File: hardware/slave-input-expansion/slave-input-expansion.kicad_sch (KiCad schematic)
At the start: 52 parts, among them J2 Conn_02x06_Odd_Even, J5 Conn_01x06, J6 ICSP, SW1 SW_Push, SW2 SW_Push, U3 PCF8574, U4 DS1233A-10

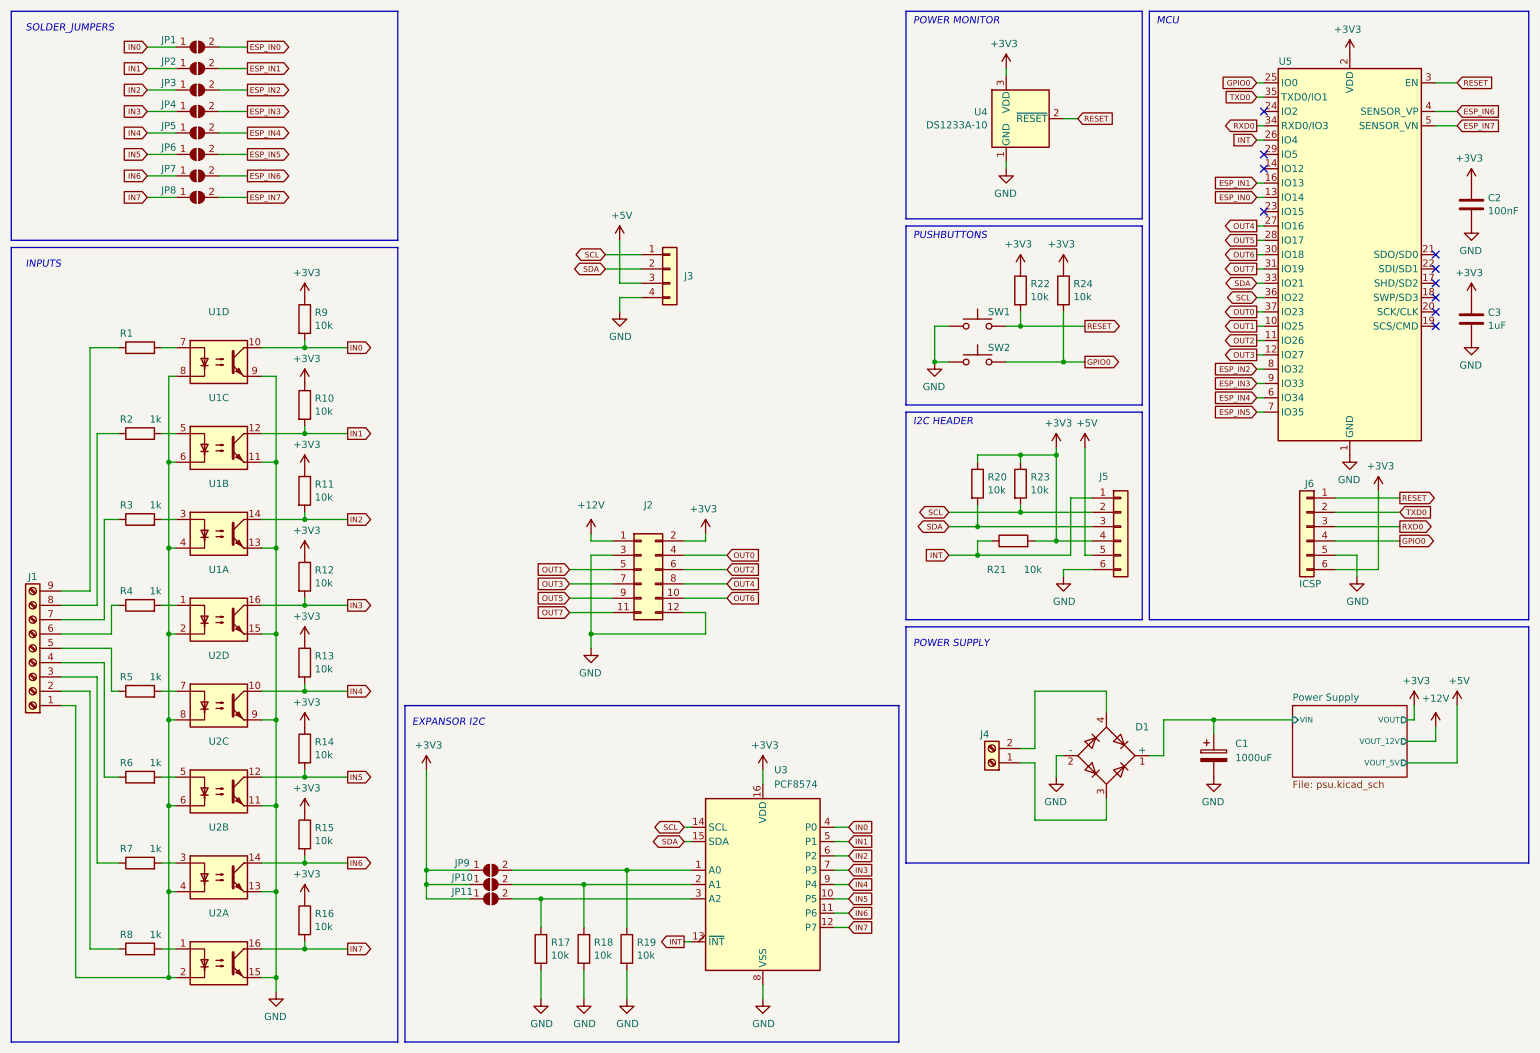
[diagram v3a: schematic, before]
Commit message: switch to 12v psu
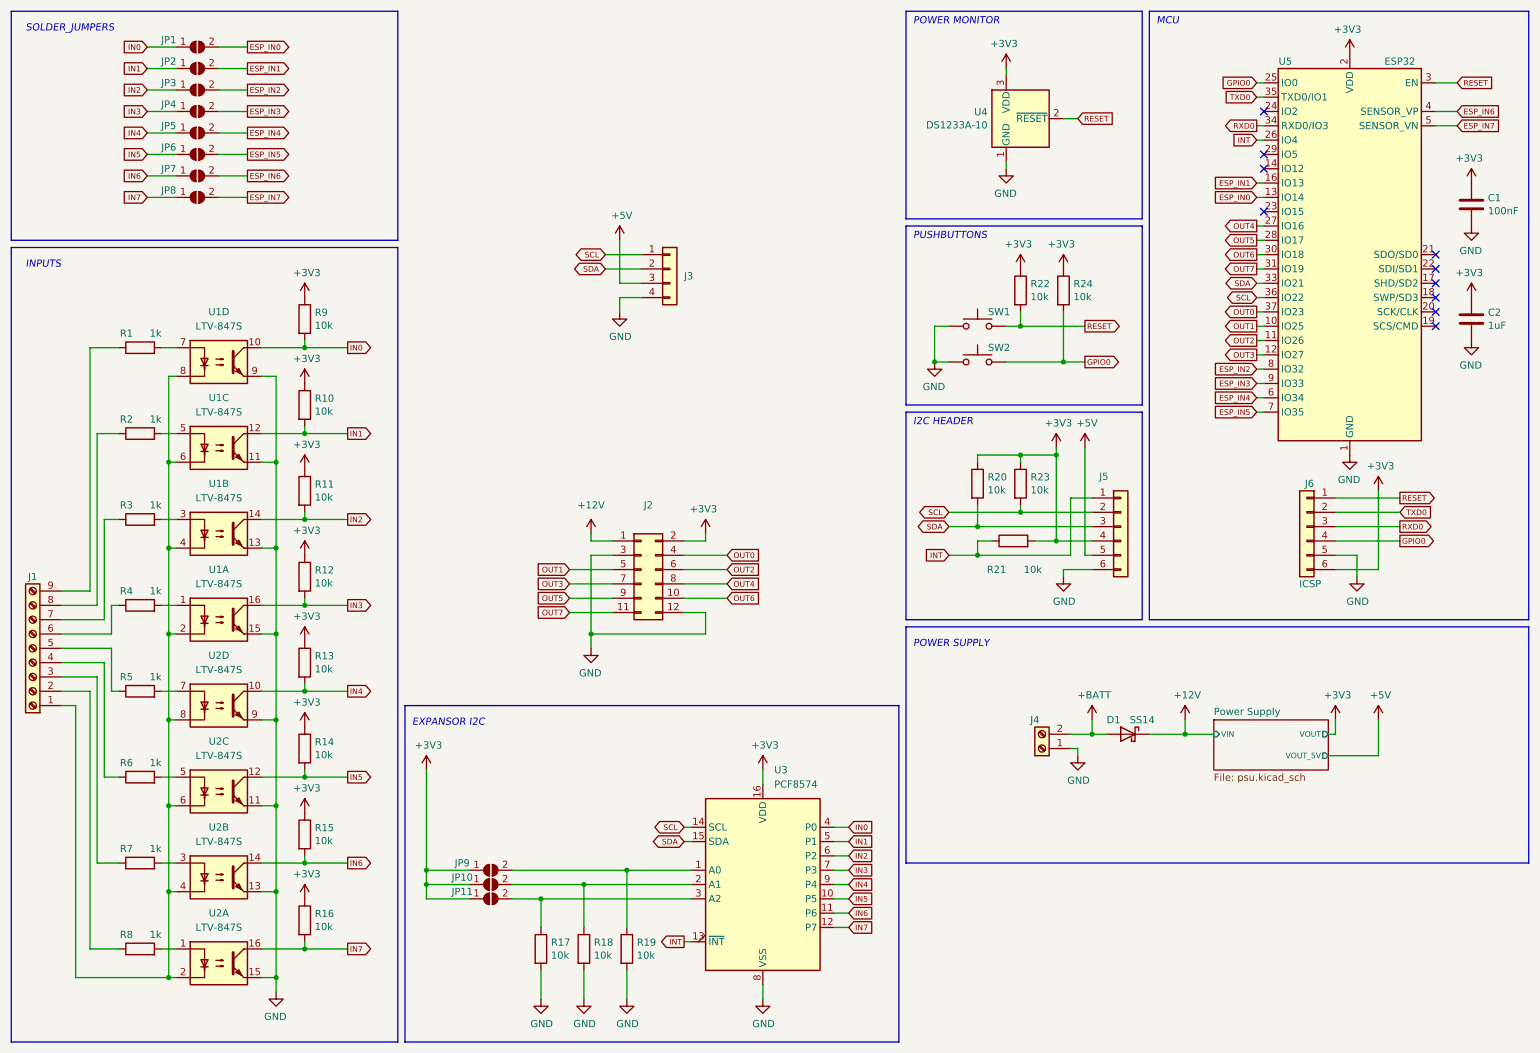
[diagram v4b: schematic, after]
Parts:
- removed C1: 1000uF, symbol Device:C_Polarized
- removed D1: (no value), symbol Diode_Bridge:ABS10
- added D1: SS14, Diode_SMD:D_SMA_Handsoldering, symbol Diode:B140-E3
- J1: value (none) -> Screw_Terminal_01x09; footprint (none) -> TerminalBlock_Phoenix:TerminalBlock_Phoenix_MKDS-1,5-9-5.08_1x09_P5.08mm_Horizontal
- J3: value (none) -> Conn_01x04; footprint (none) -> Connector_PinHeader_2.54mm:PinHeader_1x04_P2.54mm_Vertical
- J4: value (none) -> Screw_Terminal_01x02; footprint (none) -> TerminalBlock_Phoenix:TerminalBlock_Phoenix_MKDS-1,5-2-5.08_1x02_P5.08mm_Horizontal
- R1: value (none) -> 1k; footprint (none) -> Resistor_SMD:R_1206_3216Metric
- U1, U2: value (none) -> LTV-847S; footprint (none) -> Package_DIP:SMDIP-16_W9.53mm
- U5: value (none) -> ESP32; footprint (none) -> esp32-wroom-roover:ESP32-WROOM-32
- renumbered C2 to C1, C3 to C2
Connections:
- net +12V: now also D1.1 (K)
- net GND: now also J4.1 (Pin_1)
- net +BATT: now reaches J4.2 (Pin_2)
- net +BATT: now also D1.2 (A)
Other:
- sheet Power Supply ports: added none; removed VOUT_12V
- moved on the sheet: J4
